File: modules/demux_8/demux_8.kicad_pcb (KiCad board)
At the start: 2 copper layers, 21.3 x 34.3 mm, 125 parts, among them J1 Conn_02x18_Row_Letter_First, Q1 2N3904, Q10 2N3904, Q11 2N3904, Q12 2N3904, Q13 2N3904, Q14 2N3904, Q15 2N3904, Q16 2N3904, Q17 2N3904, Q18 2N3904, Q19 2N3904, Q2 2N3906, Q20 2N3904, Q21 2N3904, Q22 2N3904, Q23 2N3904, Q24 2N3904, Q25 2N3904, Q26 2N3904, Q27 2N3904, Q28 2N3904, Q29 2N3904, Q3 2N3906, Q30 2N3904, Q31 2N3904, Q32 2N3904, Q33 2N3904, Q34 2N3904, Q35 2N3904, Q36 2N3904, Q37 2N3904, Q38 2N3904, Q39 2N3904, Q4 2N3906, Q40 2N3904, Q41 2N3904, Q42 2N3904, Q43 2N3904, Q44 2N3904, Q45 2N3904, Q46 2N3904, Q47 2N3904, Q48 2N3904, Q49 2N3904, Q5 2N3904, Q50 2N3904, Q51 2N3904, Q52 2N3904, Q53 2N3904, Q54 2N3904, Q55 2N3904, Q56 2N3904, Q57 2N3904, Q58 2N3904, Q59 2N3904, Q6 2N3904, Q60 2N3904, Q7 2N3904, Q8 2N3904, Q9 2N3904

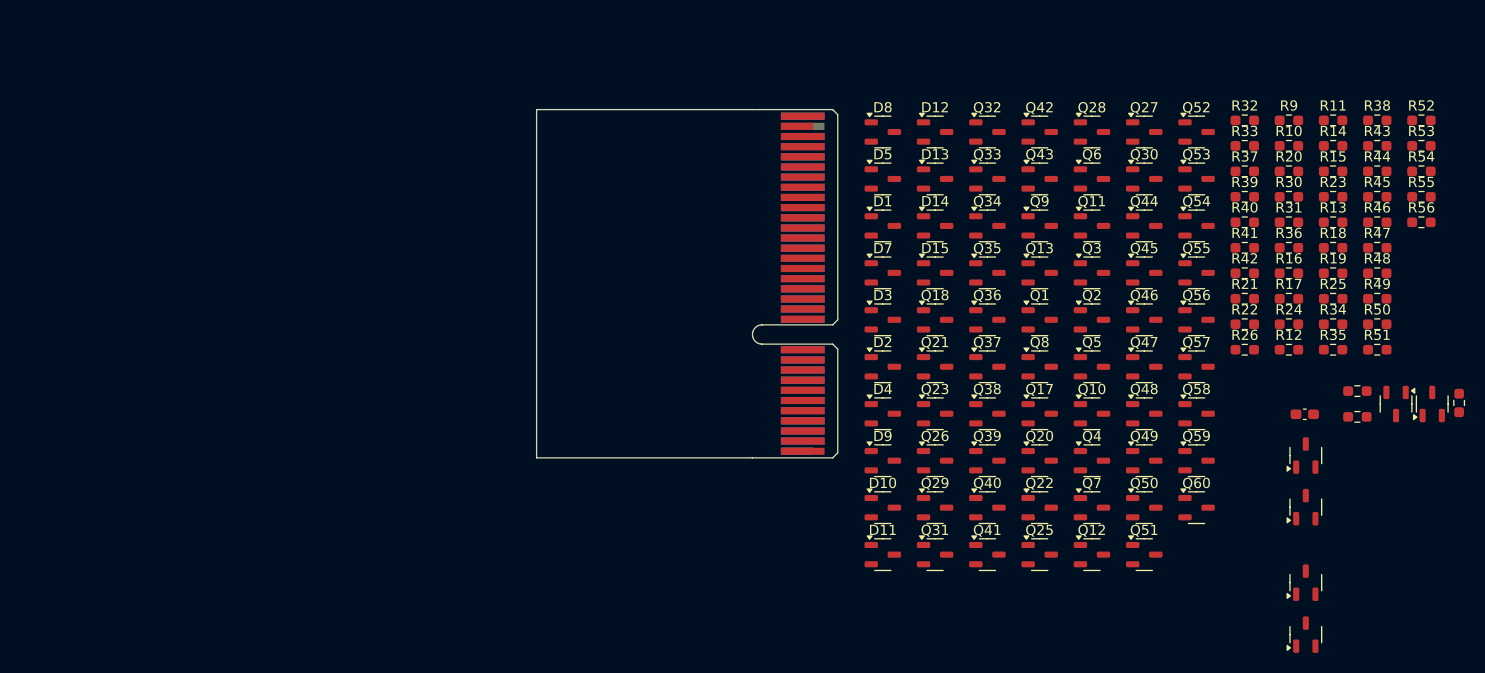
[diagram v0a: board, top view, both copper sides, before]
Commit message: Some work towards a decoder component placement.
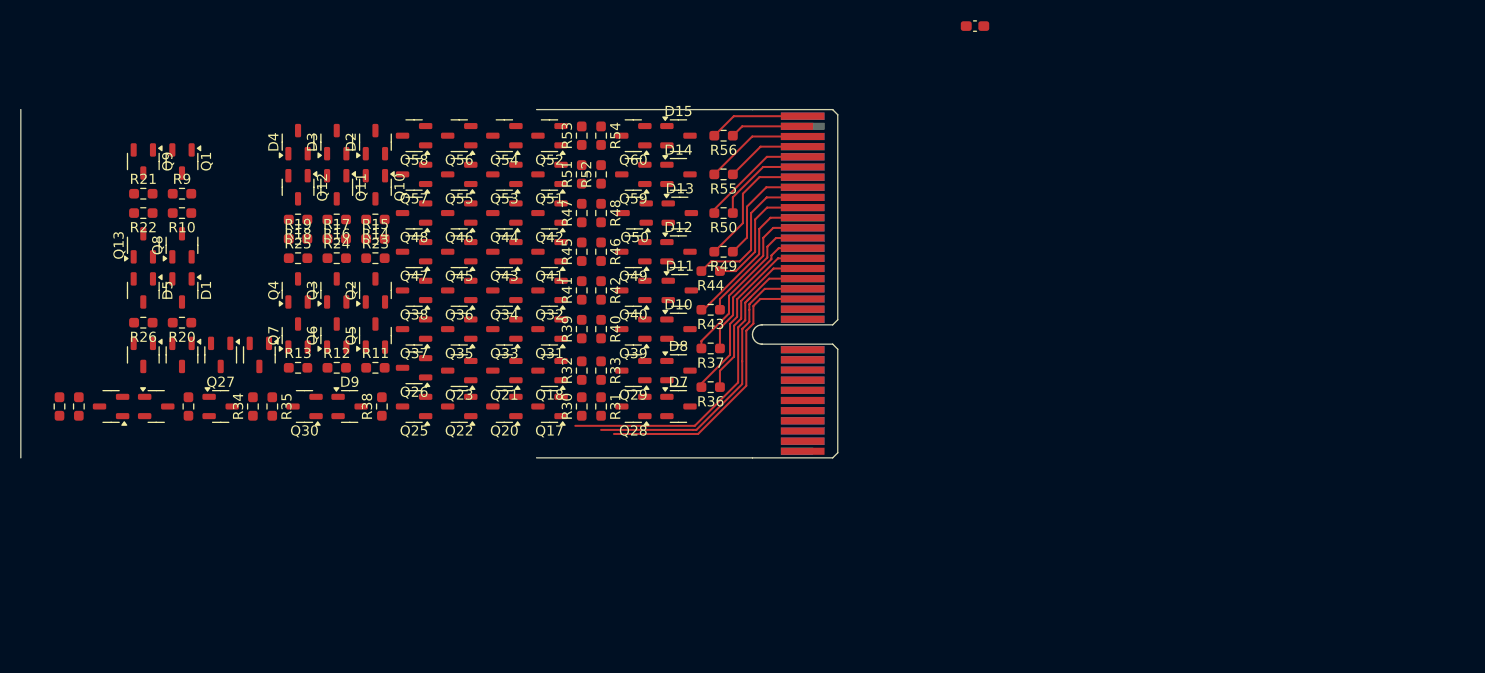
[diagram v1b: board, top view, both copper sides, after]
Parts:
- moved R27 127.8 mm to (76.2, 72.4), turned to -90 degrees
- moved Q24 126.6 mm to (81.3, 72.4), turned to 180 degrees
- moved R28 125.9 mm to (78.1, 72.4), turned to -90 degrees
- moved D6 125.7 mm to (85.7, 72.4), turned to 0 degrees
- moved R29 125.2 mm to (88.9, 72.4)
- moved Q19 117.8 mm to (84.5, 67.3), turned to -90 degrees
- moved Q16 112.9 mm to (88.3, 67.3), turned to -90 degrees
- moved R20 110.0 mm to (88.3, 64.1), turned to 180 degrees
- moved R9 109.3 mm to (88.3, 51.4)
- moved R10 109.2 mm to (88.3, 53.3), turned to 180 degrees
- moved R22 109.0 mm to (84.5, 53.3), turned to 180 degrees
- moved R21 109.0 mm to (84.5, 51.4)
- moved R26 108.5 mm to (84.5, 64.1), turned to 180 degrees
- moved Q14 107.3 mm to (92.1, 67.3), turned to -90 degrees
- moved R34 106.7 mm to (95.2, 72.4), turned to 90 degrees
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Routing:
- net /C: track 0.00 -> 33.0 mm
- net /B: track 0.00 -> 29.8 mm
- net /A: track 0.00 -> 28.3 mm
- net /O0: track 0.00 -> 18.2 mm
- net /V_O0: track 0.00 -> 16.7 mm
- net /O1: track 0.00 -> 16.6 mm
- net /O2: track 0.00 -> 15.2 mm
- net /O3: track 0.00 -> 15.1 mm
- net /V_O1: track 0.00 -> 14.6 mm
- net /O4: track 0.00 -> 13.4 mm
- net /V_O2: track 0.00 -> 13.1 mm
- net /V_O3: track 0.00 -> 12.6 mm
- net /V_O4: track 0.00 -> 11.3 mm
- net /O5: track 0.00 -> 11.2 mm
- net /O6: track 0.00 -> 10.3 mm
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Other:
- board size 21.3 x 34.3 mm -> 72.1 x 34.3 mm

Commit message: More or less finalized PCB for 8-way demux.
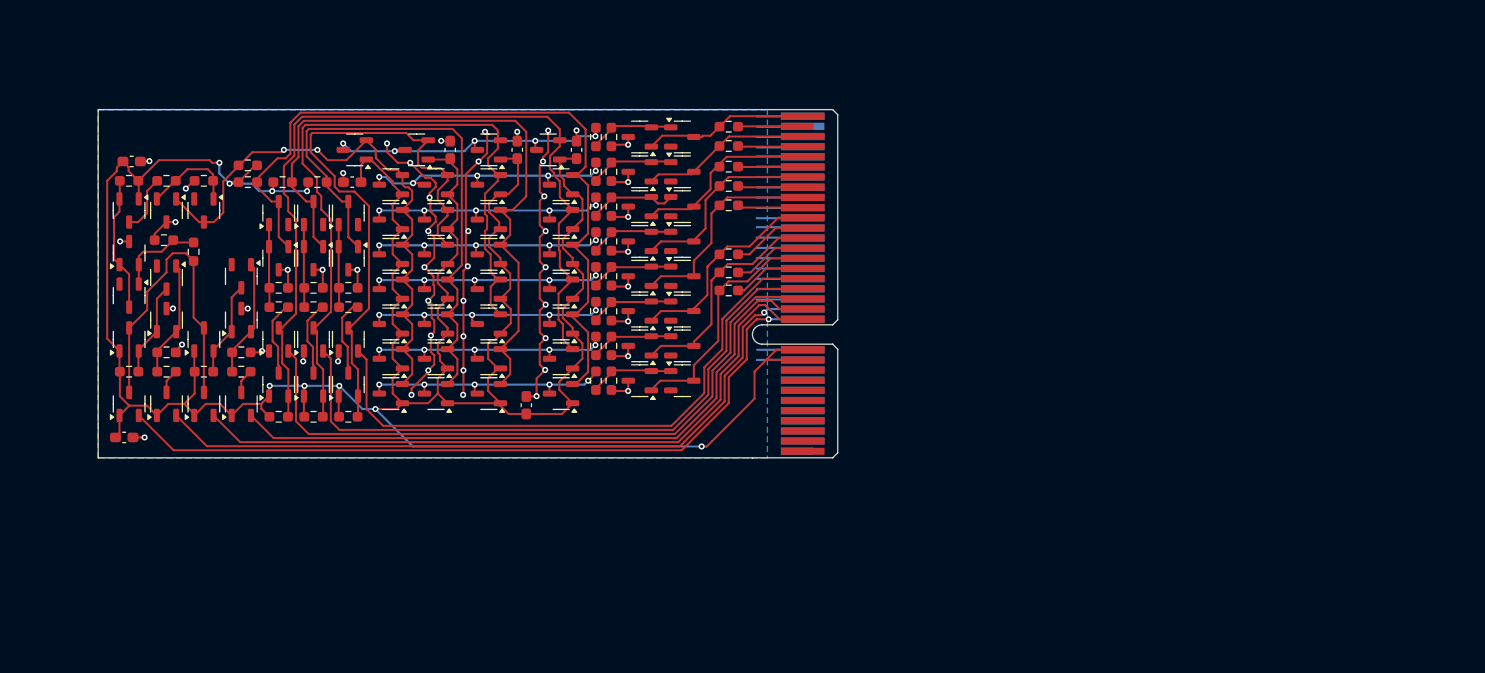
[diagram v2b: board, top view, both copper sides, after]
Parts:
- added C2: 1u, Capacitor_SMD:C_0603_1608Metric_Pad1.08x0.95mm_HandSolder, F.Cu at (127.1, 47.1)
- added C3: 1u, Capacitor_SMD:C_0603_1608Metric_Pad1.08x0.95mm_HandSolder, F.Cu at (121.3, 47.1)
- added C4: 1u, Capacitor_SMD:C_0603_1608Metric_Pad1.08x0.95mm_HandSolder, F.Cu at (105.0, 50.3)
- added C5: 1u, Capacitor_SMD:C_0603_1608Metric_Pad1.08x0.95mm_HandSolder, F.Cu at (114.7, 47.1)
- added C6: 1u, Capacitor_SMD:C_0603_1608Metric_Pad1.08x0.95mm_HandSolder, F.Cu at (83.3, 48.3)
- added C7: 1u, Capacitor_SMD:C_0603_1608Metric_Pad1.08x0.95mm_HandSolder, F.Cu at (122.2, 72.3)
- moved C1 93.1 mm to (82.6, 75.4)
- moved R38 27.2 mm to (94.7, 48.6), turned to 180 degrees
- moved Q1 24.6 mm to (94.1, 72.1), turned to 90 degrees
- moved D9 24.1 mm to (90.4, 53.1), turned to -90 degrees
- moved Q9 24.0 mm to (86.7, 72.1), turned to 90 degrees
- moved R34 23.8 mm to (86.7, 50.2), turned to 0 degrees
- moved Q30 23.6 mm to (86.7, 53.1), turned to -90 degrees
- moved R35 23.2 mm to (90.4, 50.2), turned to 180 degrees
- moved R29 23.0 mm to (83.1, 50.2), turned to 180 degrees
- moved Q27 21.3 mm to (83.1, 53.1), turned to -90 degrees
- moved R27 20.2 mm to (89.4, 57.1), turned to 90 degrees
- moved R9 18.5 mm to (94.1, 69.0), turned to 180 degrees
- moved R28 18.4 mm to (86.5, 56.0), turned to 180 degrees
- moved R21 17.7 mm to (86.7, 69.0), turned to 180 degrees
- moved Q24 15.2 mm to (83.1, 57.3), turned to 90 degrees
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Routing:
- net VCC: track 0.00 -> 302.8 mm, vias 0 -> 9
- net GND: track 0.00 -> 230.3 mm, vias 0 -> 52
- net /_A: track 0.00 -> 83.3 mm
- net /_~{A}: track 0.00 -> 76.6 mm
- net /~{EN1}: track 0.00 -> 75.4 mm, vias 0 -> 1
- net /EN3: track 0.00 -> 71.8 mm, vias 0 -> 1
- net /_B: track 0.00 -> 71.7 mm
- net /~{EN0}: track 0.00 -> 68.5 mm
- net /_~{B}: track 0.00 -> 66.6 mm
- net /EN2: track 0.00 -> 64.4 mm
- net /_C: track 0.00 -> 58.9 mm
- net /_~{C}: track 0.00 -> 56.8 mm
- net /~{EN}: track 0.00 -> 56.7 mm, vias 0 -> 2
- net /A: track 28.3 -> 66.6 mm
- net /B: track 29.8 -> 63.1 mm
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- added copper zone on B.Cu, net GND
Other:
- board size 72.1 x 34.3 mm -> 64.4 x 34.3 mm
